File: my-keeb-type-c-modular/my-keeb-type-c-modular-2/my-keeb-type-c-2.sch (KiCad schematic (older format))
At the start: 114 parts, among them J1 AVR-ISP-6, SW1 SW_Push, U1 ATmega32U4-AU, U2 PRTR5V0U2X, Y1 16MHz

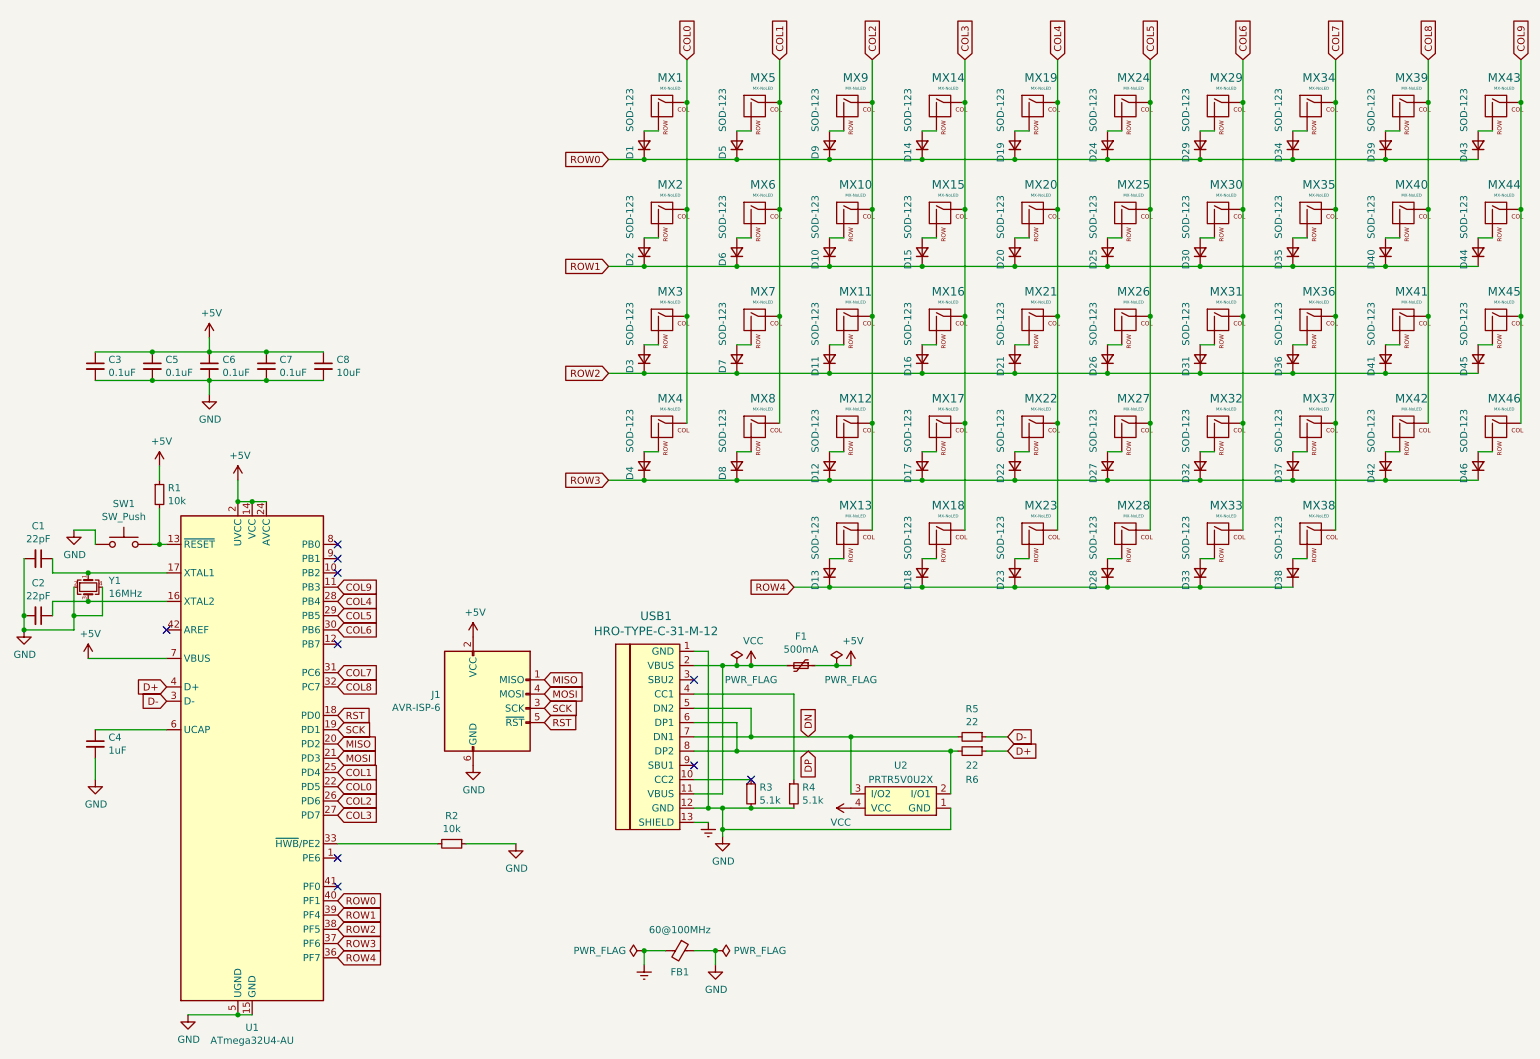
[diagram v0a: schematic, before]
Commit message: Finished type c part 2 and updated type c part 1
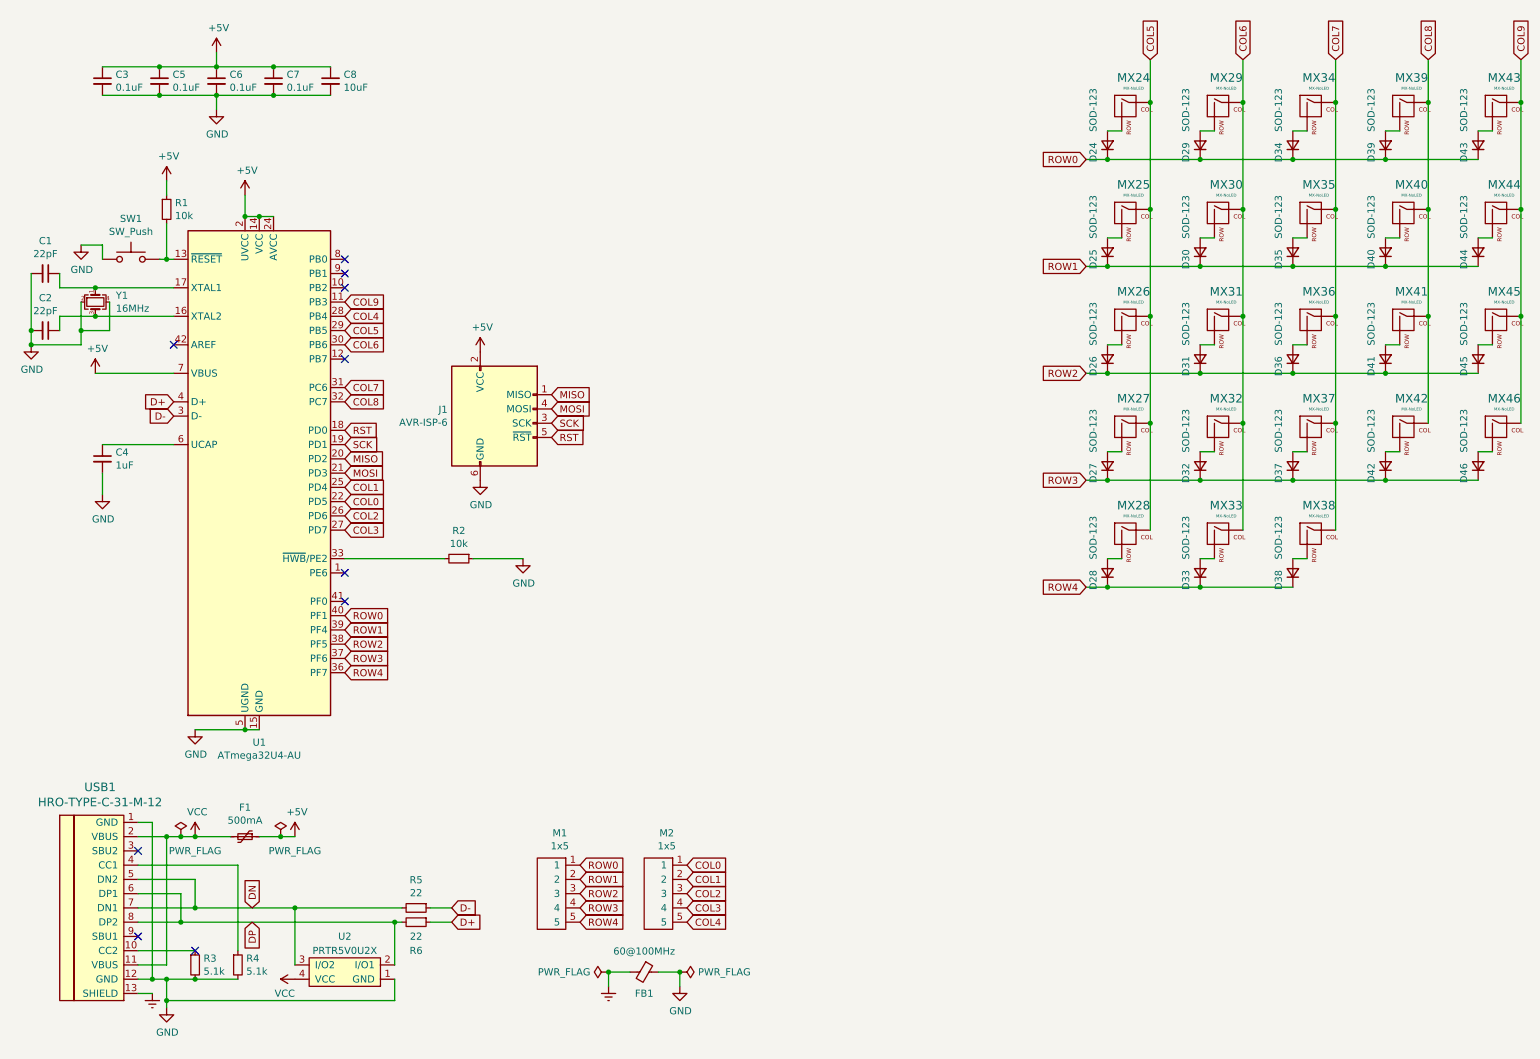
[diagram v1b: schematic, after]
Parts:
- removed D1, D10, D11, D12, D13, D14, D15, D16, D17, D18, D19, D2, D20, D21, D22, D23, D3, D4, D5, D6, D7, D8, D9: SOD-123, Diode_SMD:D_SOD-123, symbol Device:D_Small
- removed MX1, MX10, MX11, MX12, MX13, MX14, MX15, MX16, MX17, MX18, MX19, MX2, MX20, MX21, MX22, MX3, MX4, MX5, MX6, MX7, MX8, MX9: MX-NoLED, MX_Alps_Hybrid:MX-1U-NoLED, symbol MX_Alps_Hybrid:MX-NoLED
- removed MX23: MX-NoLED, MX_Alps_Hybrid:MX-1.5U-NoLED, symbol MX_Alps_Hybrid:MX-NoLED
- added M1, M2: 1x5, modular:1x5, symbol modular:1x5
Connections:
- net COL0: now also M2.1
- net COL1: now also M2.2
- net COL2: now also M2.3
- net COL3: now also M2.4
- net COL4: now also M2.5
- net ROW0: now also M1.1
- net ROW1: now also M1.2
- net ROW2: now also M1.3
- net ROW3: now also M1.4
- net ROW4: now also M1.5
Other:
- moved on the sheet: C1, C2, C3, C4, C5, C6, C7, C8, F1, FB1, J1, R1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
